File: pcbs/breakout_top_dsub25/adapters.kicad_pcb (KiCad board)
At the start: 2 copper layers, 130 x 99.5 mm, 37 parts, among them J1 Screw_Terminal_01x06, J10 f3, J11 f3, J12 f4, J13 Conn_01x04_Pin, J14 Conn_01x04_Pin, J15 Conn_01x06_Pin, J16 f4, J17 f6, J18 f6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

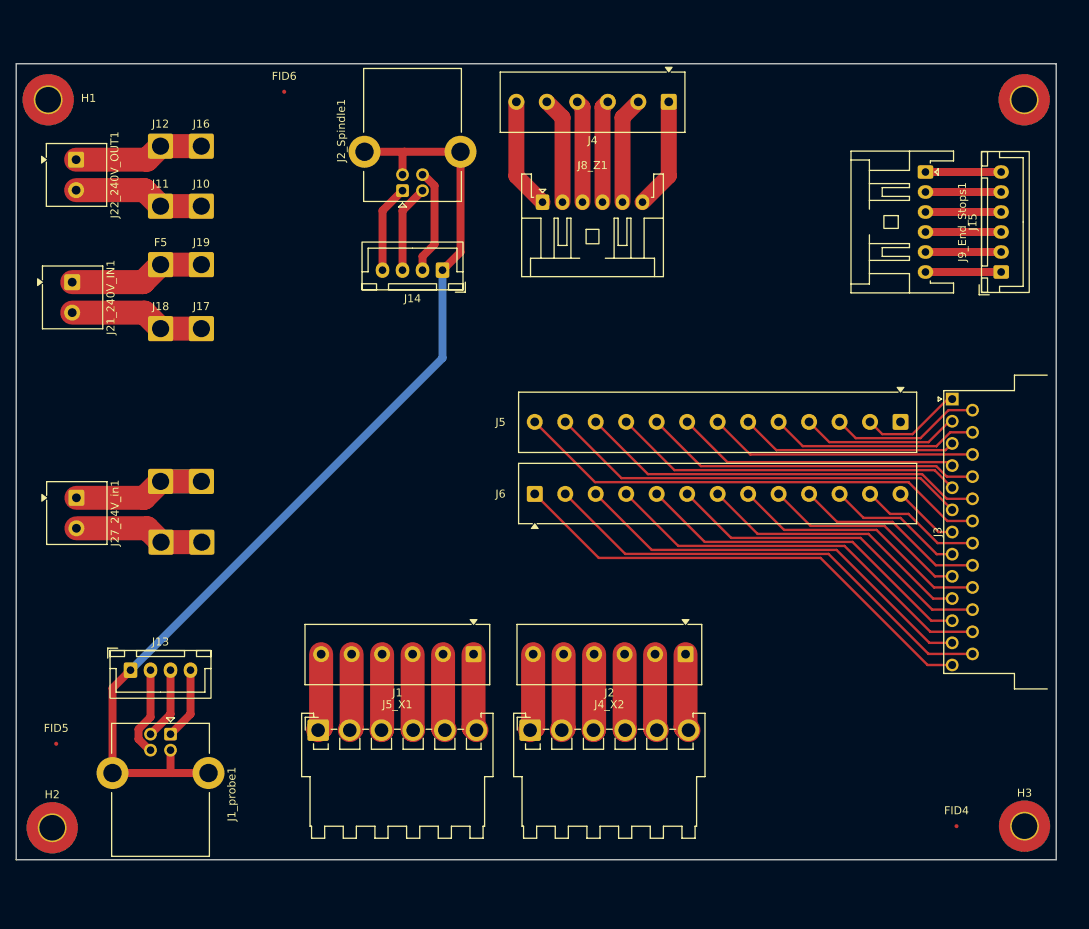
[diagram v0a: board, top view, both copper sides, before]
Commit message: adding various silk layer labels
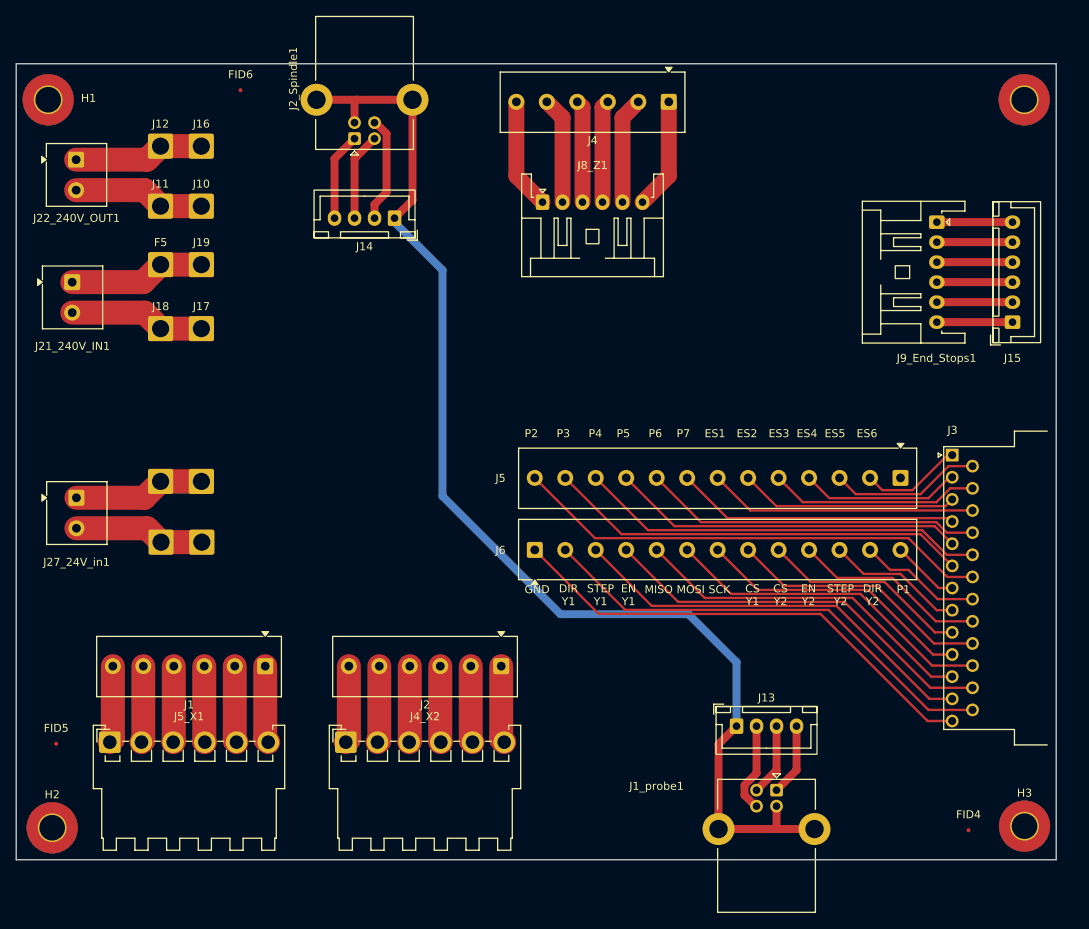
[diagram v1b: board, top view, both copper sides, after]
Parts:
- moved J13 76.1 mm to (175.0, 132.0)
- moved J1_probe1 76.1 mm to (180.0, 140.0)
- moved J5_X1 26.1 mm to (96.7, 134.0)
- moved J1 26.1 mm to (116.1, 124.5)
- moved J2 23.1 mm to (145.6, 124.5)
- moved J4_X2 23.1 mm to (126.2, 134.0)
- moved J14 8.85 mm to (132.2, 68.5)
- moved J2_Spindle1 8.85 mm to (127.2, 58.6)
- moved J3 7.00 mm to (202.0, 98.1)
- moved J5 7.00 mm to (195.5, 101.0)
- moved J6 7.00 mm to (149.8, 110.0)
- moved J9_End_Stops1 6.43 mm to (200.0, 69.0)
- moved J15 6.43 mm to (209.5, 81.5)
- moved FID6 5.46 mm to (113.0, 52.5)
- moved FID4 1.58 mm to (204.0, 145.0)
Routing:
- net GND: track 125.6 -> 150.0 mm
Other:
- board text added: "CS Y1"
- board text added: "CS Y2"
- board text added: "DIR Y1"
- board text added: "DIR Y2"
- board text added: "EN Y1"
- board text added: "EN Y2"
- board text added: "ES1"
- board text added: "ES2"
- board text added: "ES3"
- board text added: "ES4"
- board text added: "ES5"
- board text added: "ES6"
- board text added: "GND"
- board text added: "MISO"
- board text added: "MOSI"
- board text added: "P1"
- board text added: "P2"
- board text added: "P3"
- board text added: "P4"
- board text added: "P5"
- board text added: "P6"
- board text added: "P7"
- board text added: "SCK"
- board text added: "STEP Y1"
- board text added: "STEP Y2"

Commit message: tweak top board
add mounting holes in the middle (enable zip for cables?)
reposition a few components
fix some rules warnings
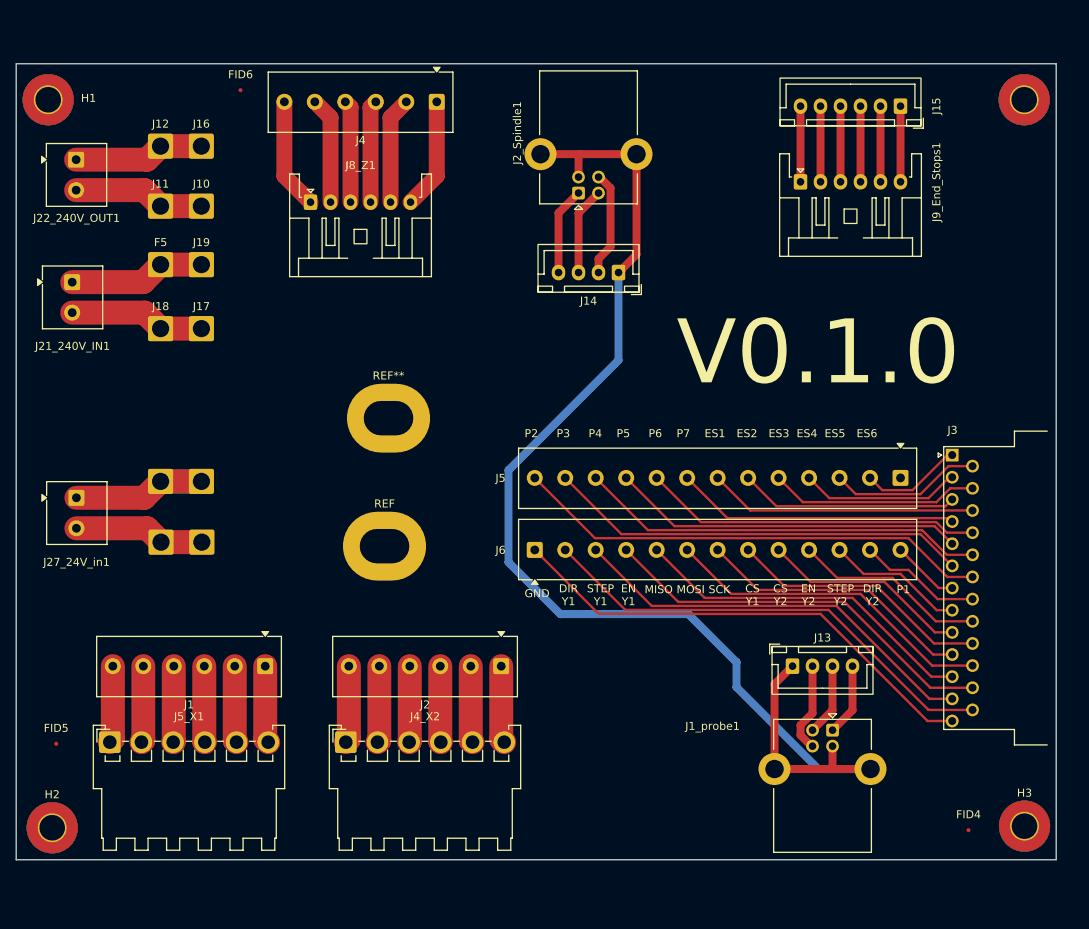
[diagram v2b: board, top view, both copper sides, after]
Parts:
- added REF: MountingHole_4.3x6.2mm_M4_Pad, MountingHole:MountingHole_4.3x6.2mm_M4_Pad, F.Cu at (131.0, 109.5)
- added REF**: MountingHole_4.3x6.2mm_M4_Pad, MountingHole:MountingHole_4.3x6.2mm_M4_Pad, F.Cu at (131.5, 93.5)
- moved J15 30.4 mm to (195.5, 54.5), turned to 180 degrees
- moved J4 29.0 mm to (137.5, 54.0)
- moved J8_Z1 29.0 mm to (121.8, 66.5)
- moved J14 28.8 mm to (160.2, 75.3)
- moved J2_Spindle1 28.8 mm to (155.2, 65.4)
- moved J9_End_Stops1 17.8 mm to (183.0, 64.0), turned to 0 degrees
- moved J13 10.3 mm to (182.0, 124.5)
- moved J1_probe1 10.3 mm to (187.0, 132.5)
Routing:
- net GND: track 150.0 -> 159.1 mm
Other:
- board text added: "V0.1.0"

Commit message: adding ground plan
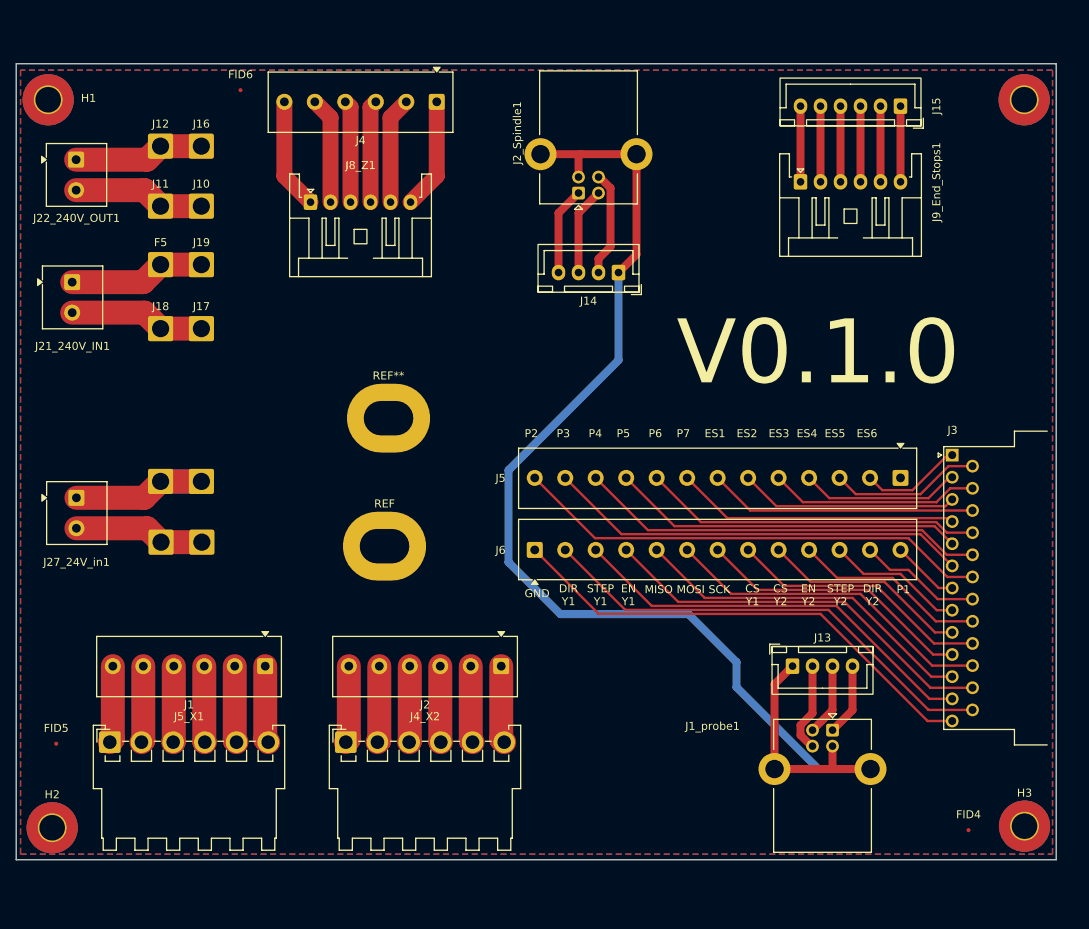
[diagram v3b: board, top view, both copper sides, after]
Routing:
- added copper zone on B.Cu, net GND
- added copper zone on F.Cu, net GND
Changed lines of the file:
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@@
 		(net "Net-(J4-Pin_6)")
+	)
+	(zone
+		(net "GND")
+		(layer "F.Cu")
+		(hatch none 0.5)
+		(priority 1)
+		(connect_pads
+			(clearance 0.5)
+		)
+		(min_thickness 0.25)
+		(fill yes
+			(thermal_gap 0.5)
+			(thermal_bridge_width 0.5)
+			(island_removal_mode 0)
+		)
+		(polygon
+			(pts
+				(xy 85.5 50) (xy 85.5 148) (xy 214.5 148) (xy 214.5 50)
+			)
+		)
+	)
+	(zone
+		(net "GND")
+		(layer "B.Cu")
+		(hatch edge 0.5)
+		(connect_pads
+			(clearance 0.5)
+		)
+		(min_thickness 0.25)
+		(fill yes
+			(thermal_gap 0.5)
+			(thermal_bridge_width 0.5)
+			(island_removal_mode 0)
+		)
+		(polygon
+			(pts
+				(xy 85.5 50) (xy 85.5 148) (xy 214.5 148) (xy 214.5 50)
+			)
+		)
 	)
 	(embedded_fonts no)

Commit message: add version/name
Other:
- board text added: "YetiCNC Revival - Top - v0.1 Kakwalab © - 2026"
- board text removed: "V0.1.0"
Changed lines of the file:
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@@
 		)
 	)
-	(gr_text "V0.1.0"
-		(at 167.5 90 0)
+	(gr_text "YetiCNC Revival - Top - v0.1\nKakwalab © - 2026"
+		(at 173.5 91.5 0)
 		(layer "F.SilkS")
 		(effects
 			(font
-				(size 8 8)
-				(thickness 0.1)
+				(size 3 3)
+				(thickness 0.3)
 			)
-			(justify left bottom)
+			(justify bottom)
 		)
 	)

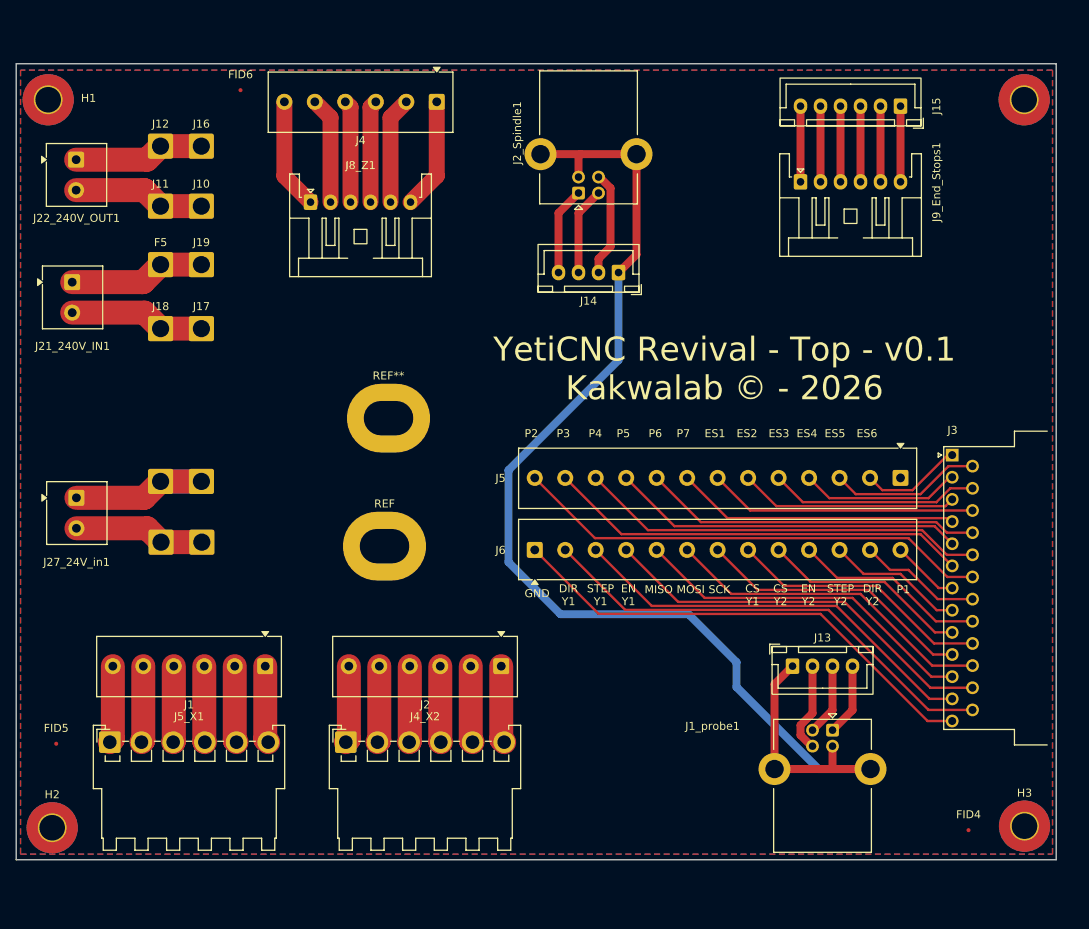
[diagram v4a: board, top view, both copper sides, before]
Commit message: relabel dsub 25 pins which were rewired/renumbered for 24V routing + add spacing for power supply stuff.
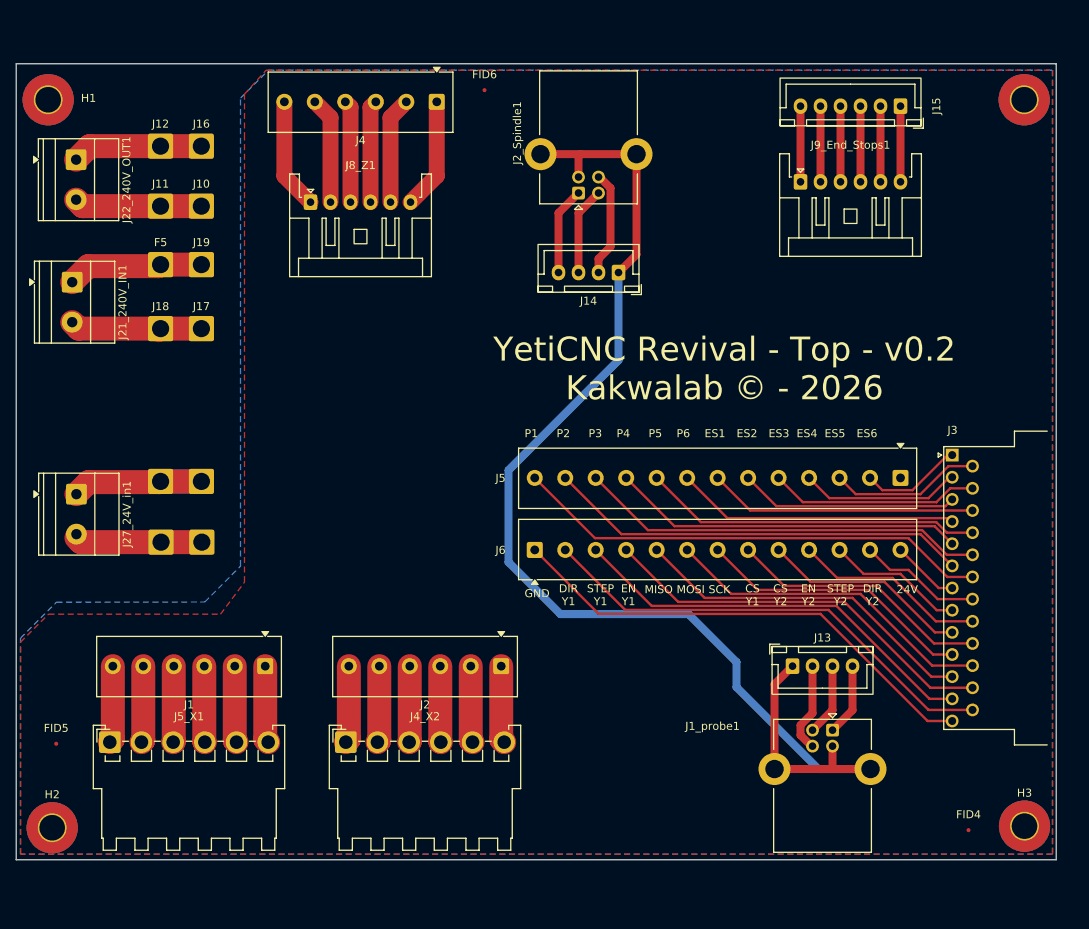
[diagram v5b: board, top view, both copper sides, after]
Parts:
- removed REF, REF**: MountingHole_4.3x6.2mm_M4_Pad, MountingHole:MountingHole_4.3x6.2mm_M4_Pad
- J21_240V_IN1, J22_240V_OUT1, J27_24V_in1: footprint TerminalBlock_Phoenix:TerminalBlock_Phoenix_MKDS-1-2-3.81_1x02_P3.81mm_Horizontal -> TerminalBlock_Phoenix:TerminalBlock_Phoenix_MKDS-1,5-2_1x02_P5.00mm_Horizontal
- J8_Z1, J9_End_Stops1: footprint Connector_JST:JST_XA_S06B-XASK-1_1x06_P2.50mm_Horizontal -> Connector_JST:JST_XA_S06B-XASK-1N-BN_1x06_P2.50mm_Horizontal
- moved FID6 30.5 mm to (143.5, 52.5)
- moved J27_24V_in1 0.46 mm to (92.5, 103.0)
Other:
- board text added: "24V"
- board text added: "YetiCNC Revival - Top - v0.2 Kakwalab © - 2026"
- board text removed: "P7"
- board text removed: "YetiCNC Revival - Top - v0.1 Kakwalab © - 2026"
